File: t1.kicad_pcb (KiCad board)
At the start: 4 copper layers, 63 x 35.6 mm, 47 parts, among them J1 Barrel_Jack_Switch, J2 USB_B, J3 P1, J4 2x2M, J5 ICSP1, J6 P2, U1 ATmega8U2-AU, Y1 16MHz

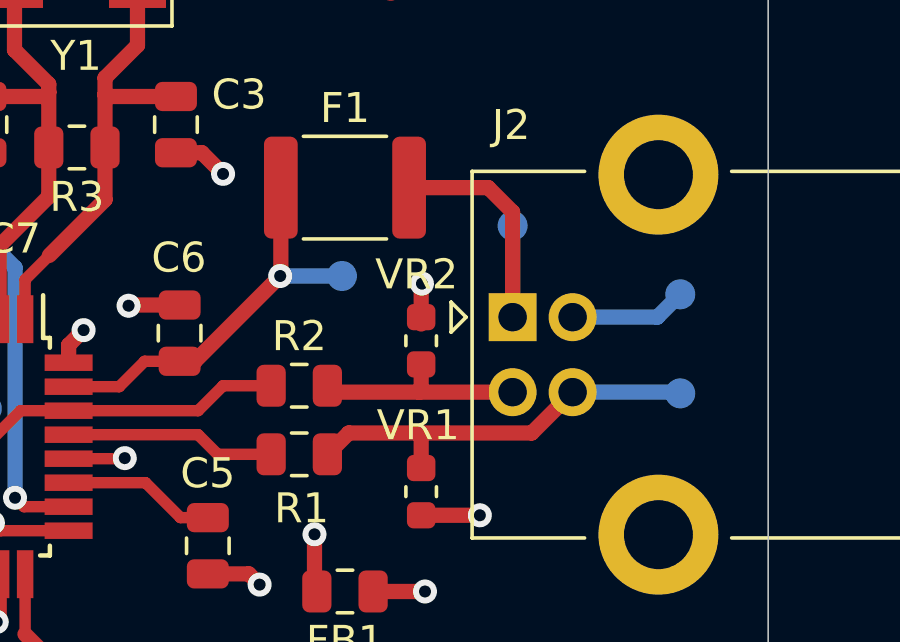
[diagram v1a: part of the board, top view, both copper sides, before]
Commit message: Migrated to KiCad 7
Also introduced some changes to get diffs
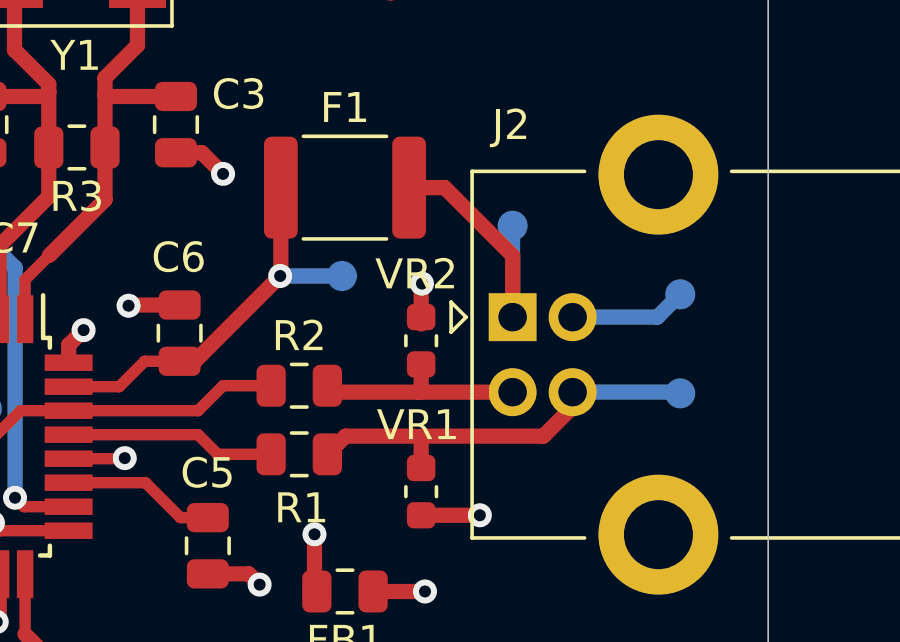
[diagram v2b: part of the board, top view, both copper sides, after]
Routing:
- net Net-(F1-Pad2): track 10.3 -> 9.49 mm
